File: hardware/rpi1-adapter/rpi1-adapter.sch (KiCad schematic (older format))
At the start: 16 parts, among them P1 I2C, P2 CONN_02X13, P3 UART, P4 CONN_02X08, P5 relays, P6 5V, U1 OPTO-TRANSISTOR-4, U2 OPTO-TRANSISTOR-4

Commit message: o more on adapter. Add DC/DC converter to only need one 12V supply.
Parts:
- removed P4: CONN_02X08, Pin_Headers:Pin_Header_Straight_2x08, symbol CONN_02X08
- added C1: 110p, Capacitors_SMD:C_0805_HandSoldering, symbol C
- added C2, C5: 100n, Capacitors_SMD:C_0805_HandSoldering, symbol C
- added C3: 100u, Capacitors_ThroughHole:C_Radial_D10_L16_P5, symbol CP
- added C4: 100u, Capacitors_SMD:C_1206_HandSoldering, symbol CP
- added D1: D_Schottky_Small, Diodes_SMD:Diode-SMA_Handsoldering, symbol D_Schottky_Small
- added L1: L_Small, Inductors:INDUCTOR_V, symbol L_Small
- added P4, P7, P8: CONN_01X08, terminal:TerminalBlock-8pin-3.5mm, symbol CONN_01X08
- added P9: CONN_01X04, symbol CONN_01X04
- added R10: 1k, Resistors_SMD:R_0805_HandSoldering, symbol R
- added R11: 3k, Resistors_SMD:R_0805_HandSoldering, symbol R
- added R9: 0R3, Resistors_SMD:R_0805_HandSoldering, symbol R
- added U3: MC34063, Housings_SOIC:SOIC-8_3.9x4.9mm_Pitch1.27mm, symbol MC34063
- P6: value 5V -> 12V; footprint Pin_Headers:Pin_Header_Straight_1x02 -> Connect:JACK_ALIM
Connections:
- net labels added: +12V
- wire segments 46 -> 81
- no-connect marks 0 -> 5
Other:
- note added: "Back from realays: 12V switched."
- note added: "Connector towards Raspberry Pi"
- note added: "Output to relays"
- moved on the sheet: P1, P2, P3, P5, P6, U2A, U2B, U2C, U2D

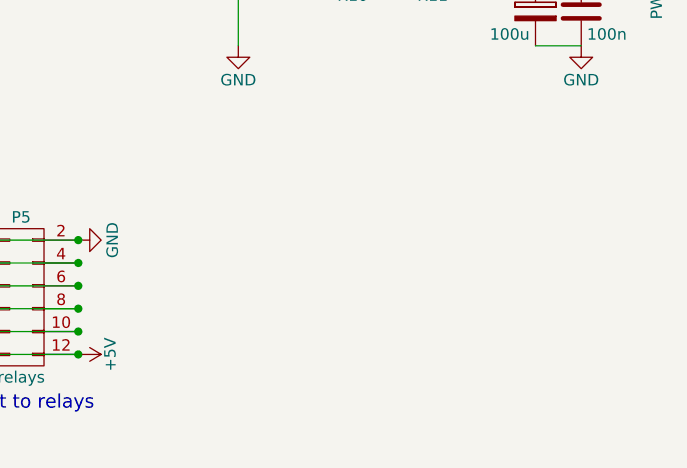
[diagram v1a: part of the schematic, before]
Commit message: o Add dual P-mosfet to be used.
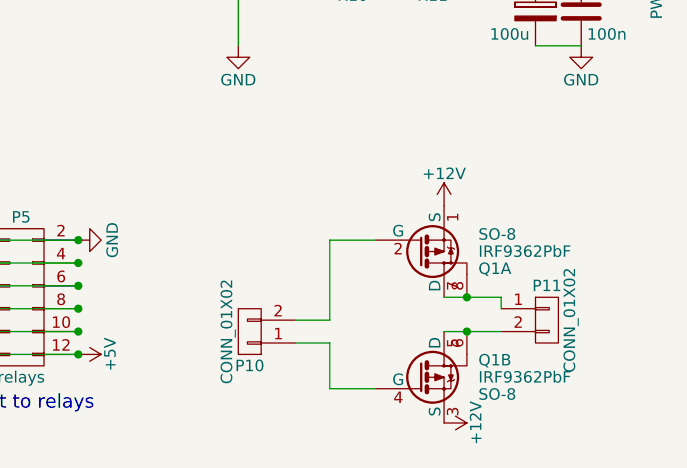
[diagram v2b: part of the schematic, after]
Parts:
- added P10, P11: CONN_01X02, Pin_Headers:Pin_Header_Straight_1x02, symbol CONN_01X02
- added Q1: IRF9362PbF, SO-8, symbol IRF9362PbF
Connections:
- net +12V: now also Q1.1 (S), Q1.3 (S)
- new net: P10.1 (P1), Q1.4 (G)
- new net: P10.2 (P2), Q1.2 (G)
- new net: P11.1 (P1), Q1.7 (D), Q1.8
- new net: P11.2 (P2), Q1.5 (D), Q1.6

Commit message: o work in progress..
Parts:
- removed P10, P11: CONN_01X02, Pin_Headers:Pin_Header_Straight_1x02, symbol CONN_01X02
- removed P5: relays, Pin_Headers:Pin_Header_Straight_2x06, symbol CONN_02X06
- removed P9: CONN_01X04, symbol CONN_01X04
- added D10, D11, D4, D5, D6, D7, D8, D9: Led_Small, LEDs:LED-0805, symbol Led_Small
- added D2, D3: D, Diodes_ThroughHole:Diode_DO-35_SOD27_Horizontal_RM10, symbol D
- added Q2: IRF9362PbF, Power_Integrations:SO-8, symbol IRF9362PbF
- added R12, R13, R14, R15: 180, Resistors_SMD:R_0805_HandSoldering, symbol R
- added R16, R17, R18, R19: R, Resistors_SMD:R_0805_HandSoldering, symbol R
- added U4: OPTO-TRANSISTOR-4, Housings_DIP:DIP-16_W7.62mm_LongPads, symbol OPTO-TRANSISTOR-4
- P4: value CONN_01X08 -> Sensors 1
- P7: value CONN_01X08 -> Sensors 2
- P8: value CONN_01X08 -> 12V actor outputs
- Q1: footprint SO-8 -> Power_Integrations:SO-8
- R1, R2, R3, R4, R5, R6, R7, R8: value R -> 1k2; footprint Resistors_ThroughHole:Resistor_Vertical_RM5mm -> Resistors_SMD:R_0805_HandSoldering
- U1, U2: footprint (none) -> Housings_DIP:DIP-16_W7.62mm_LongPads
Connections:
- net +12V: now also R1.1, R2.1, R3.1, R4.1, R5.1, R6.1, R7.1, R8.1, D2.1 (K), Q2.1 (S), Q2.3 (S), R16.1, R17.1, R18.1, R19.1; no longer C2.2, C3.1, P6.2 (P2), R9.2, U3.6 (VCC)
- net +5V: no longer R1.1, R2.1, R3.1, R4.1, R5.1, R6.1, R7.1, R8.1
- net GND: now also U4.11, U4.13, U4.15, U4.2, U4.4, U4.6, U4.8, U4.9
- net in-11: now also U2.10; no longer U2.16
- net in-17: now also U1.10; no longer U1.16
- net in-18: now also U2.12; no longer U2.14
- net in-21: now also U1.14; no longer U1.12
- net in-22: now also U1.12; no longer U1.14
- net in-23: now also U2.14; no longer U2.12
- net in-24: now also U2.16; no longer U2.10
- net in-4: now also U1.16; no longer U1.10
- net out-10: now also R15.2
- net out-7: now also R12.2
- net out-8: now also R13.2
- net out-9: now also R14.2
- net at U2.1: now also D6.1 (K); no longer R1.2
- net at U2.2: now also P4.2 (P2); no longer P4.8 (P8)
- net at U2.3: now also D5.1 (K); no longer R2.2
- net at U2.4: now also P4.4 (P4); no longer P4.6 (P6)
- net at U2.5: now also D4.1 (K); no longer R3.2
- net at U2.6: now also P4.6 (P6); no longer P4.4 (P4)
- net at U2.7: now also D8.1 (K); no longer R4.2
- net at U2.8: now also P4.8 (P8); no longer P4.2 (P2)
- net at U1.1: now also D11.1 (K); no longer R5.2
- net at U1.2: now also P7.2 (P2); no longer P7.8 (P8)
- net at U1.3: now also D10.1 (K); no longer R6.2
- net at U1.4: now also P7.4 (P4); no longer P7.6 (P6)
- net at U1.5: now also D9.1 (K); no longer R7.2
- net at U1.6: now also P7.6 (P6); no longer P7.4 (P4)
- net at U1.7: no longer R8.2
- net at U1.8: now also P7.8 (P8); no longer P7.2 (P2)
- net at P8.2 (P2): now also Q1.5 (D), Q1.6
- net at P8.4 (P4): now also Q1.7 (D), Q1.8
- net at P8.6 (P6): now also Q2.5 (D), Q2.6
- net at P8.8 (P8): now also Q2.7 (D), Q2.8
- net at Q1.4 (G): now also R16.2, U4.10
- net at Q1.2 (G): now also R17.2, U4.12
- new net: C2.2, C3.1, D3.1 (K), R9.2, U3.6 (VCC)
- new net: Q2.2 (G), R19.2, U4.16
- new net: Q2.4 (G), R18.2, U4.14
- new net: R15.1, U4.1
- new net: R14.1, U4.3
- new net: R13.1, U4.5
- new net: R12.1, U4.7
- new net: D8.2 (A), R1.2
- new net: D4.2 (A), R2.2
- new net: D5.2 (A), R3.2
- new net: D6.2 (A), R4.2
- new net: D7.2 (A), R5.2
- new net: D9.2 (A), R6.2
- new net: D10.2 (A), R7.2
- new net: D11.2 (A), R8.2
- new net PowerIn: D2.2 (A), D3.2 (A), P6.2 (P2)
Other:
- note added: "4 high-side switches."
- note removed: "Back from realays: 12V switched."
- note removed: "Output to relays"
- moved on the sheet: P8, U1A, U1B, U1C, U1D, U2A, U2B, U2C, U2D

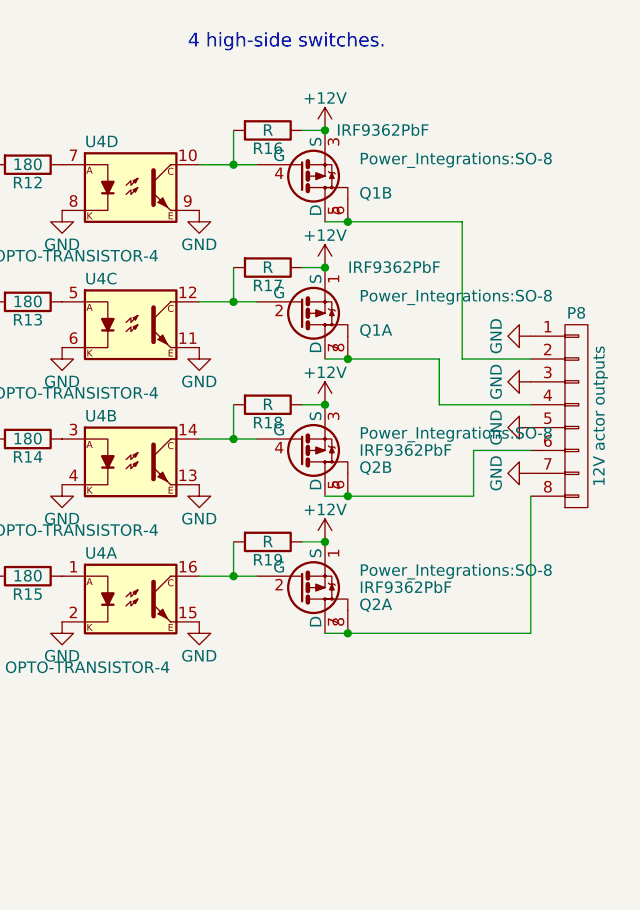
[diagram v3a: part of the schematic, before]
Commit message: o Add free-wheel diodes.
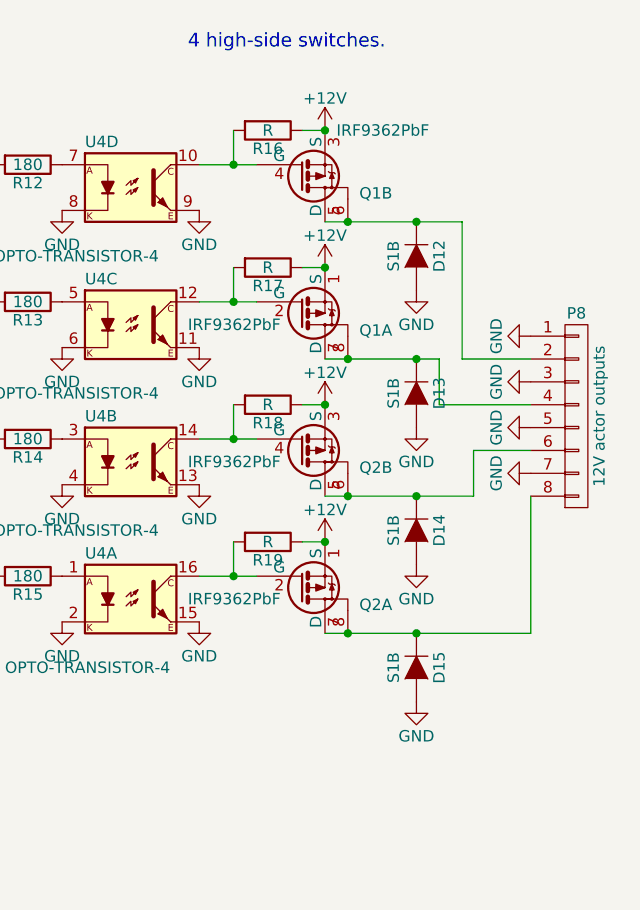
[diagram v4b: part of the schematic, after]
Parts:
- added D12, D13, D14, D15: S1B, Diodes_SMD:Diode-SMA_Standard, symbol D
- R4: footprint Resistors_SMD:R_0805_HandSoldering -> Resistors_SMD:R_0805
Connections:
- net GND: now also D12.2 (A), D13.2 (A), D14.2 (A), D15.2 (A)
- net at P8.2 (P2), Q1.5 (D), Q1.6: now also D12.1 (K)
- net at P8.4 (P4), Q1.7 (D), Q1.8: now also D13.1 (K)
- net at P8.6 (P6), Q2.5 (D), Q2.6: now also D14.1 (K)
- net at P8.8 (P8), Q2.7 (D), Q2.8: now also D15.1 (K)
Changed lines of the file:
@@
 $EndComp
 $Comp
-L GND #PWR48
+L GND #PWR52
 U 1 1 55808095
 P 10300 2200
-F 0 "#PWR48" H 10300 1950 50  0001 C CNN
+F 0 "#PWR52" H 10300 1950 50  0001 C CNN
 F 1 "GND" H 10300 2050 50  0000 C CNN
 F 2 "" H 10300 2200 60  0000 C CNN
@@
 $EndComp
 $Comp
-L GND #PWR49
+L GND #PWR53
 U 1 1 558081D8
 P 10300 2400
-F 0 "#PWR49" H 10300 2150 50  0001 C CNN
+F 0 "#PWR53" H 10300 2150 50  0001 C CNN
 F 1 "GND" H 10300 2250 50  0000 C CNN
 F 2 "" H 10300 2400 60  0000 C CNN
@@
 $EndComp
 $Comp
-L GND #PWR50
+L GND #PWR54
 U 1 1 5580822B
 P 10300 2600
-F 0 "#PWR50" H 10300 2350 50  0001 C CNN
+F 0 "#PWR54" H 10300 2350 50  0001 C CNN
 F 1 "GND" H 10300 2450 50  0000 C CNN
 F 2 "" H 10300 2600 60  0000 C CNN
@@
 $EndComp
 $Comp
-L GND #PWR51
+L GND #PWR55
 U 1 1 5580827E
 P 10300 2800
-F 0 "#PWR51" H 10300 2550 50  0001 C CNN
+F 0 "#PWR55" H 10300 2550 50  0001 C CNN
 F 1 "GND" H 10300 2650 50  0000 C CNN
 F 2 "" H 10300 2800 60  0000 C CNN
@@
 P 9300 2100
 F 0 "Q1" H 9550 2175 50  0000 L CNN
-F 1 "IRF9362PbF" H 9500 1900 50  0000 L CNN
-F 2 "Power_Integrations:SO-8" H 9550 2025 50  0000 L CNN
+F 1 "IRF9362PbF" H 8800 2150 50  0000 L CNN
+F 2 "Power_Integrations:SO-8" H 9550 2025 50  0001 L CNN
 F 3 "" H 9300 2100 50  0000 L CNN
 	1    9300 2100
@@
 F 0 "Q1" H 9550 1575 50  0000 L CNN
 F 1 "IRF9362PbF" H 9450 1300 50  0000 L CNN
-F 2 "Power_Integrations:SO-8" H 9550 1425 50  0000 L CNN
+F 2 "Power_Integrations:SO-8" H 9550 1425 50  0001 L CNN
 F 3 "" H 9300 1500 50  0000 L CNN
 	2    9300 1500
@@
 P 9300 3300
 F 0 "Q2" H 9550 3375 50  0000 L CNN
-F 1 "IRF9362PbF" H 9550 3300 50  0000 L CNN
-F 2 "Power_Integrations:SO-8" H 9550 3225 50  0000 L CNN
+F 1 "IRF9362PbF" H 8800 3350 50  0000 L CNN
+F 2 "Power_Integrations:SO-8" H 9550 3225 50  0001 L CNN
 F 3 "" H 9300 3300 50  0000 L CNN
 	1    9300 3300
@@
 P 9300 2700
 F 0 "Q2" H 9550 2775 50  0000 L CNN
-F 1 "IRF9362PbF" H 9550 2700 50  0000 L CNN
-F 2 "Power_Integrations:SO-8" H 9550 2625 50  0000 L CNN
+F 1 "IRF9362PbF" H 8800 2750 50  0000 L CNN
+F 2 "Power_Integrations:SO-8" H 9550 2625 50  0001 L CNN
 F 3 "" H 9300 2700 50  0000 L CNN
 	2    9300 2700
@@
 F 0 "R4" V 2730 3300 50  0000 C CNN
 F 1 "1k2" V 2650 3300 50  0000 C CNN
-F 2 "Resistors_SMD:R_0805_HandSoldering" V 2580 3300 30  0001 C CNN
+F 2 "Resistors_SMD:R_0805" V 2580 3300 30  0001 C CNN
 F 3 "" H 2650 3300 30  0000 C CNN
 	1    2650 3300
@@
 Wire Wire Line
 	2100 4800 2350 4800
+$Comp
+L D D12
+U 1 1 5585070D
+P 9800 1850
+F 0 "D12" H 9800 1950 50  0000 C CNN
+F 1 "S1B" H 9800 1750 50  0000 C CNN
+F 2 "Diodes_SMD:Diode-SMA_Standard" H 9800 1850 60  0001 C CNN
+F 3 "" H 9800 1850 60  0000 C CNN
+	1    9800 1850
+	0    1    1    0
+$EndComp
+$Comp
+L D D13
+U 1 1 558514D7
+P 9800 2450
+F 0 "D13" H 9800 2550 50  0000 C CNN
+F 1 "S1B" H 9800 2350 50  0000 C CNN
+F 2 "Diodes_SMD:Diode-SMA_Standard" H 9800 2450 60  0001 C CNN
+F 3 "" H 9800 2450 60  0000 C CNN
+	1    9800 2450
+	0    1    1    0
+$EndComp
+$Comp
+L D D14
+U 1 1 558515C9
+P 9800 3050
+F 0 "D14" H 9800 3150 50  0000 C CNN
+F 1 "S1B" H 9800 2950 50  0000 C CNN
+F 2 "Diodes_SMD:Diode-SMA_Standard" H 9800 3050 60  0001 C CNN
+F 3 "" H 9800 3050 60  0000 C CNN
+	1    9800 3050
+	0    1    1    0
+$EndComp
+$Comp
+L D D15
+U 1 1 558516B6
+P 9800 3650
+F 0 "D15" H 9800 3750 50  0000 C CNN
+F 1 "S1B" H 9800 3550 50  0000 C CNN
+F 2 "Diodes_SMD:Diode-SMA_Standard" H 9800 3650 60  0001 C CNN
+F 3 "" H 9800 3650 60  0000 C CNN
+	1    9800 3650
+	0    1    1    0
+$EndComp
+$Comp
+L GND #PWR48
+U 1 1 558519A0
+P 9800 2000
+F 0 "#PWR48" H 9800 1750 50  0001 C CNN
+F 1 "GND" H 9800 1850 50  0000 C CNN
+F 2 "" H 9800 2000 60  0000 C CNN
+F 3 "" H 9800 2000 60  0000 C CNN
+	1    9800 2000
+	1    0    0    -1
+$EndComp
+$Comp
+L GND #PWR49
+U 1 1 55851AAB
+P 9800 2600
+F 0 "#PWR49" H 9800 2350 50  0001 C CNN
+F 1 "GND" H 9800 2450 50  0000 C CNN
+F 2 "" H 9800 2600 60  0000 C CNN
+F 3 "" H 9800 2600 60  0000 C CNN
+	1    9800 2600
+	1    0    0    -1
+$EndComp
+$Comp
+L GND #PWR50
+U 1 1 55851B76
+P 9800 3200
+F 0 "#PWR50" H 9800 2950 50  0001 C CNN
+F 1 "GND" H 9800 3050 50  0000 C CNN
+F 2 "" H 9800 3200 60  0000 C CNN
+F 3 "" H 9800 3200 60  0000 C CNN
+	1    9800 3200
+	1    0    0    -1
+$EndComp
+$Comp
+L GND #PWR51
+U 1 1 55851C41
+P 9800 3800
+F 0 "#PWR51" H 9800 3550 50  0001 C CNN
+F 1 "GND" H 9800 3650 50  0000 C CNN
+F 2 "" H 9800 3800 60  0000 C CNN
+F 3 "" H 9800 3800 60  0000 C CNN
+	1    9800 3800
+	1    0    0    -1
+$EndComp
+Connection ~ 9800 1700
+Connection ~ 9800 2300
+Connection ~ 9800 2900
+Connection ~ 9800 3500
 $EndSCHEMATC

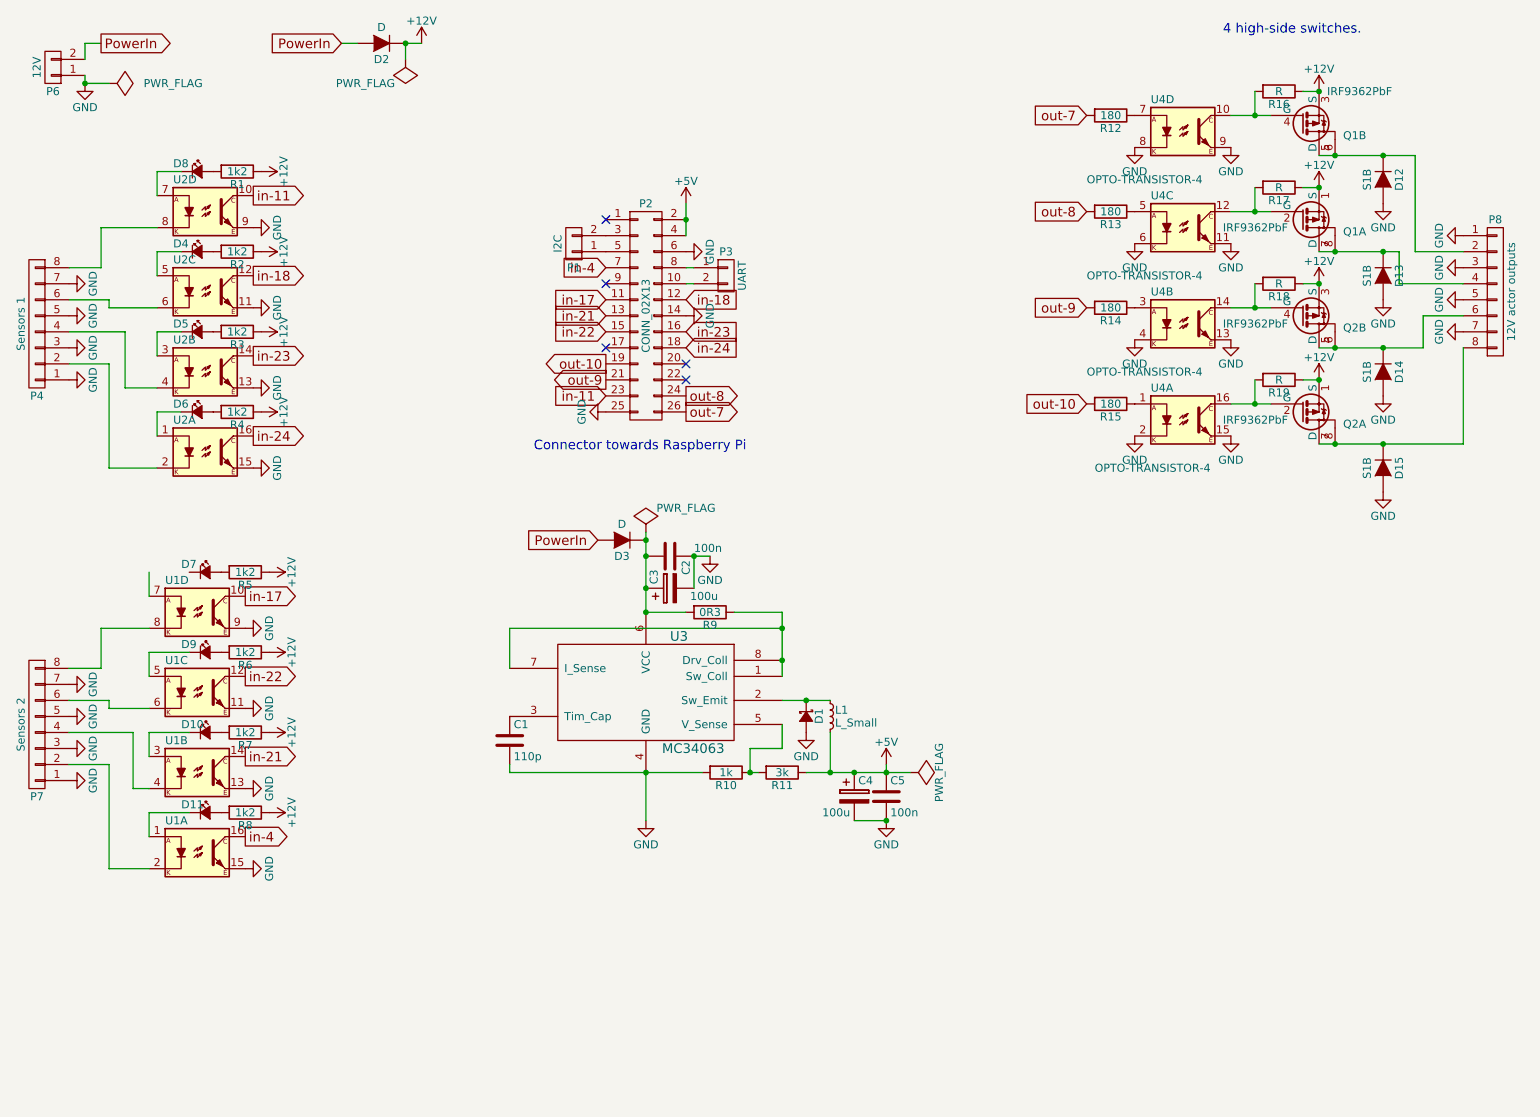
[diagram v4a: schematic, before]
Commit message: o little schematic update.
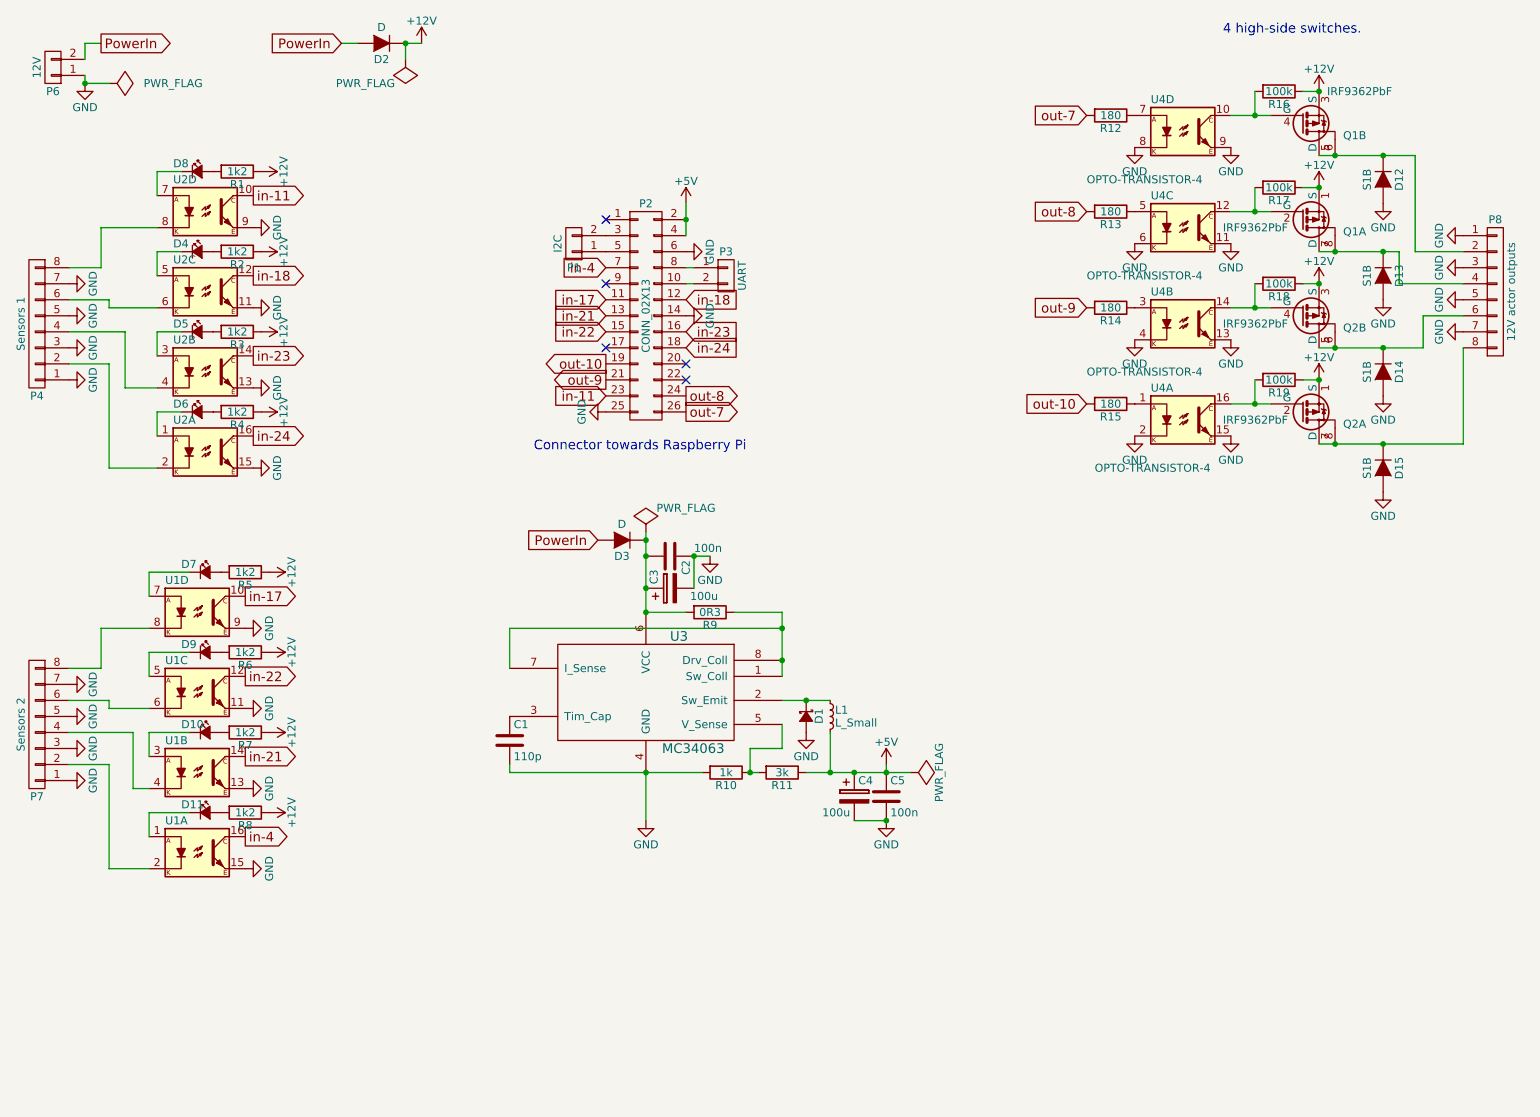
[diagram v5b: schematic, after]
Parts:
- R16, R17, R18, R19: value R -> 100k
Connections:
- net at U1.7: now also D7.1 (K)
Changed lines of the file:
@@
 P 9150 1900
 F 0 "R17" V 9230 1900 50  0000 C CNN
-F 1 "R" V 9150 1900 50  0000 C CNN
+F 1 "100k" V 9150 1900 50  0000 C CNN
 F 2 "Resistors_SMD:R_0805_HandSoldering" V 9080 1900 30  0001 C CNN
 F 3 "" H 9150 1900 30  0000 C CNN
@@
 P 9150 1300
 F 0 "R16" V 9230 1300 50  0000 C CNN
-F 1 "R" V 9150 1300 50  0000 C CNN
+F 1 "100k" V 9150 1300 50  0000 C CNN
 F 2 "Resistors_SMD:R_0805_HandSoldering" V 9080 1300 30  0001 C CNN
 F 3 "" H 9150 1300 30  0000 C CNN
@@
 P 9150 2500
 F 0 "R18" V 9230 2500 50  0000 C CNN
-F 1 "R" V 9150 2500 50  0000 C CNN
+F 1 "100k" V 9150 2500 50  0000 C CNN
 F 2 "Resistors_SMD:R_0805_HandSoldering" V 9080 2500 30  0001 C CNN
 F 3 "" H 9150 2500 30  0000 C CNN
@@
 P 9150 3100
 F 0 "R19" V 9230 3100 50  0000 C CNN
-F 1 "R" V 9150 3100 50  0000 C CNN
+F 1 "100k" V 9150 3100 50  0000 C CNN
 F 2 "Resistors_SMD:R_0805_HandSoldering" V 9080 3100 30  0001 C CNN
 F 3 "" H 9150 3100 30  0000 C CNN
@@
 Connection ~ 9800 2900
 Connection ~ 9800 3500
+Wire Wire Line
+	2100 4300 2350 4300
 $EndSCHEMATC
